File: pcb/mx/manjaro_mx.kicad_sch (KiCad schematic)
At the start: 93 parts, among them SW1 SW_Push, SW10 SW_Push, SW11 SW_Push, SW12 SW_Push, SW13 SW_Push, SW14 SW_Push, SW15 SW_Push, SW16 SW_Push, SW17 SW_Push, SW18 SW_Push, SW19 SW_Push, SW2 SW_Push, SW20 SW_Push, SW21 SW_Push, SW22 SW_Push, SW3 SW_Push, SW4 SW_Push, SW5 SW_Push, SW6 SW_Push, SW7 SW_Push, SW8 SW_Push, SW9 SW_Push, U1 XIAO-RP2040-DIP

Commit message: [V0] add jlcpcb files
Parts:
- BT1, rBT1, rJ3: now not fitted; now left out of the parts list
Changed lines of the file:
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@@
 		(unit 1)
 		(exclude_from_sim no)
-		(in_bom yes)
+		(in_bom no)
 		(on_board yes)
-		(dnp no)
+		(dnp yes)
 		(property "Reference" "rJ3"
 			(at 220.98 160.02 0)
@@
 		(unit 1)
 		(exclude_from_sim no)
-		(in_bom yes)
+		(in_bom no)
 		(on_board yes)
-		(dnp no)
+		(dnp yes)
 		(fields_autoplaced yes)
 		(property "Reference" "BT1"
@@
 		(unit 1)
 		(exclude_from_sim no)
-		(in_bom yes)
+		(in_bom no)
 		(on_board yes)
-		(dnp no)
+		(dnp yes)
 		(fields_autoplaced yes)
 		(property "Reference" "rBT1"

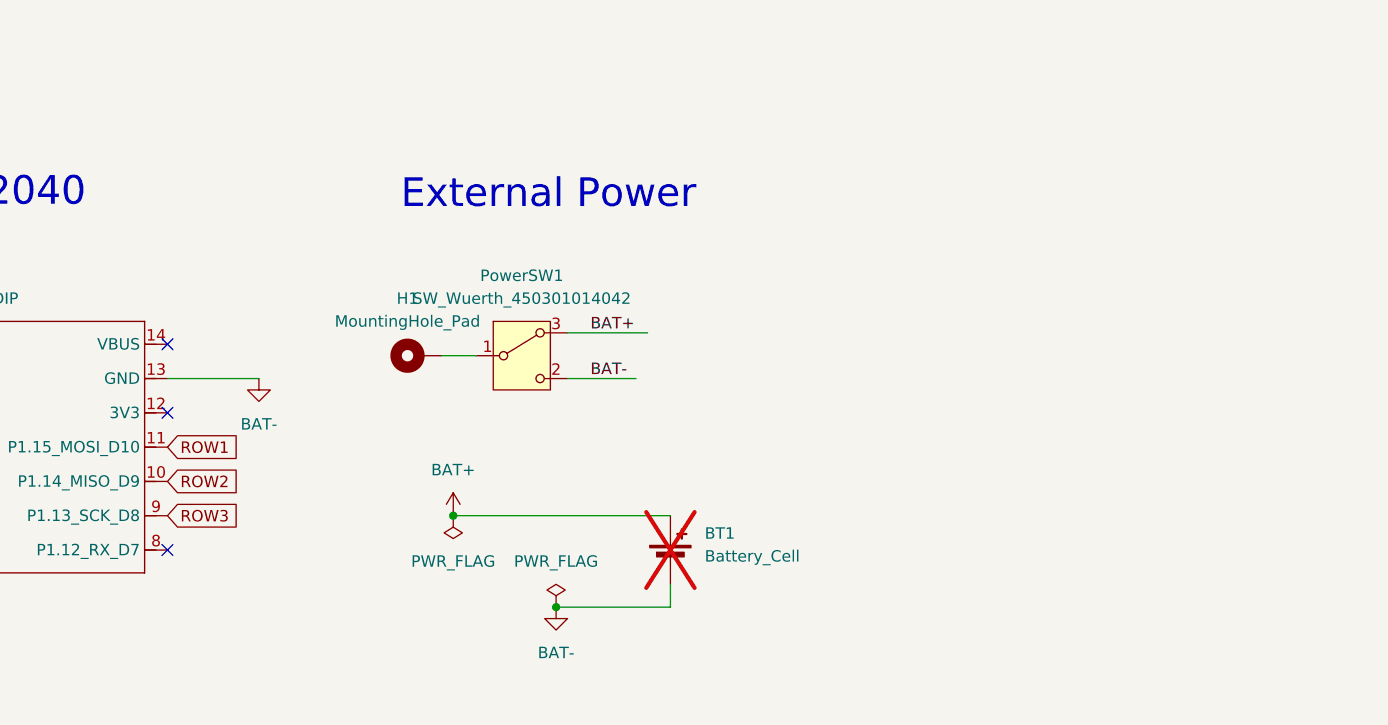
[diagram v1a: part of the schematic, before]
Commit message: [V0] Add TRRS conn for mint right
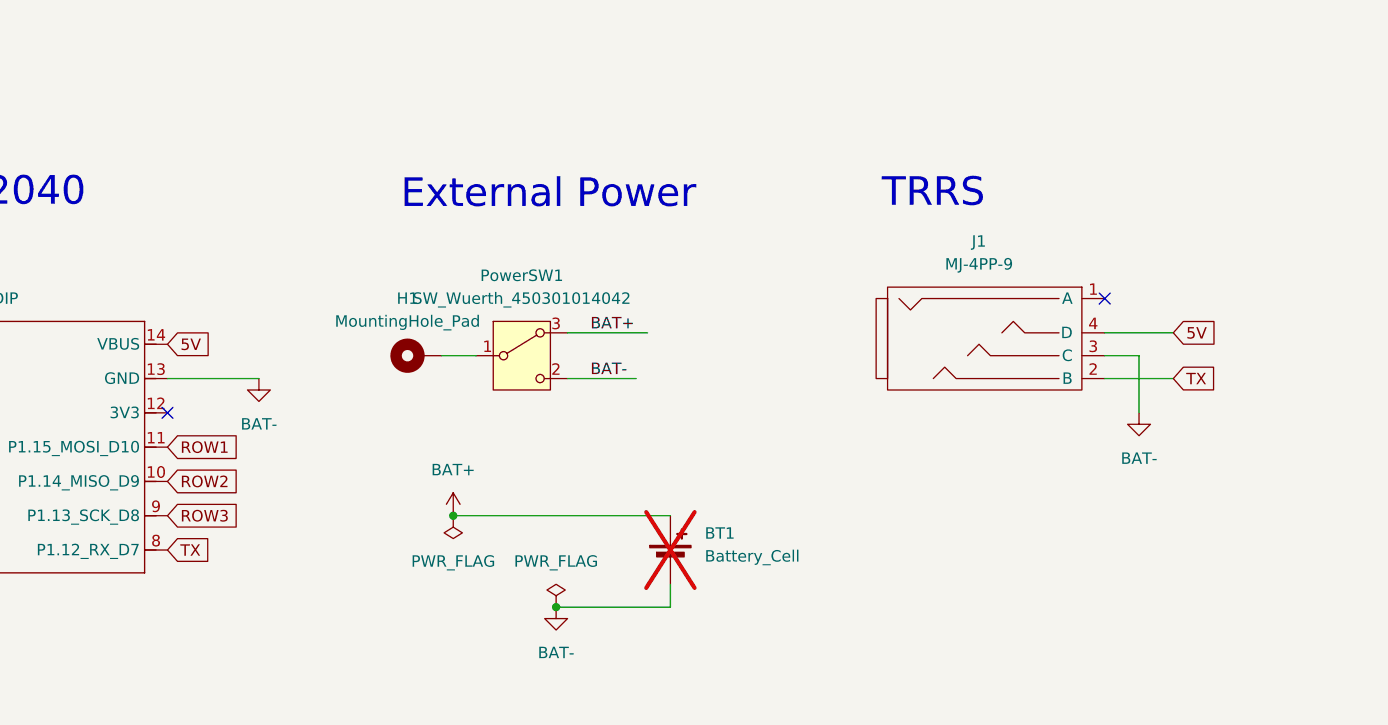
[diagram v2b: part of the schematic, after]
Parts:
- added J1: MJ-4PP-9, MJ-4PP-9:MJ-4PP-9, symbol MJ-4PP-9:MJ-4PP-9
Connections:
- net BAT-: now also J1.3 (C)
- net 5V: now reaches U1.14 (VBUS)
- net 5V: now also J1.4 (D)
- net TX: now reaches U1.8 (P1.12_RX_D7)
- net TX: now also J1.2 (B)
- no-connect marks 5 -> 4
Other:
- note added: "TRRS"

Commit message: Modify key layout
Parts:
- removed H1, H2: MountingHole_Pad, symbol Mechanical:MountingHole_Pad
- removed J1: MJ-4PP-9, MJ-4PP-9:MJ-4PP-9, symbol MJ-4PP-9:MJ-4PP-9
- removed U1, rU1: XIAO-RP2040-DIP, Seeed Studio XIAO Series Library:XIAO-RP2040-DIP, symbol Seeed_Studio_XIAO_Series:XIAO-nRF52840-DIP
- removed rD19, rD20: 1N4148WT, Diode_SMD:D_SOD-523, symbol Diode:1N4148WT
- removed rSW19, rSW20: SW_Push, kbd:keyswitch_cherrymx_hotswap_1u, symbol Switch:SW_Push
- added D23, D24, rD12, rD21, rD22, rD6: 1N4148WT, digikey-footprints:SOD-523, symbol Diode:1N4148WT
- added SW23, SW24, rSW12, rSW21, rSW22, rSW6: SW_Push, kbd_SW:CherryMX_Choc_Hotswap_1u, symbol Switch:SW_Push
- added U1, rU1: nice_nano, nice-nano-kicad:nice_nano, symbol nice_nano:nice_nano
- D1, D10, D11, D12, D13, D14, D15, D16, D17, D18, D19, D2, D20, D21, D22, D3, D4, D5, D6, D7, D8, D9, rD1, rD18, rD2, rD3, rD4, rD5: footprint Diode_SMD:D_SOD-523 -> digikey-footprints:SOD-523
- SW1, SW10, SW11, SW12, SW13, SW14, SW15, SW16, SW17, SW18, SW19, SW2, SW20, SW21, SW22, SW3, SW4, SW5, SW6, SW7, SW8, SW9, rSW1, rSW18, rSW2, rSW3, rSW4, rSW5: footprint kbd:keyswitch_cherrymx_hotswap_1u -> kbd_SW:CherryMX_Choc_Hotswap_1u
- rD10: renamed from rD9; footprint Diode_SMD:D_SOD-523 -> digikey-footprints:SOD-523
- rD11: renamed from rD10; footprint Diode_SMD:D_SOD-523 -> digikey-footprints:SOD-523
- rD13: renamed from rD11; footprint Diode_SMD:D_SOD-523 -> digikey-footprints:SOD-523
- rD14: renamed from rD12; footprint Diode_SMD:D_SOD-523 -> digikey-footprints:SOD-523
- rD15: renamed from rD13; footprint Diode_SMD:D_SOD-523 -> digikey-footprints:SOD-523
- rD16: renamed from rD14; footprint Diode_SMD:D_SOD-523 -> digikey-footprints:SOD-523
- rD17: renamed from rD15; footprint Diode_SMD:D_SOD-523 -> digikey-footprints:SOD-523
- rD19: renamed from rD16; footprint Diode_SMD:D_SOD-523 -> digikey-footprints:SOD-523
- rD20: renamed from rD17; footprint Diode_SMD:D_SOD-523 -> digikey-footprints:SOD-523
- rD7: renamed from rD6; footprint Diode_SMD:D_SOD-523 -> digikey-footprints:SOD-523
- rD8: renamed from rD7; footprint Diode_SMD:D_SOD-523 -> digikey-footprints:SOD-523
- rD9: renamed from rD8; footprint Diode_SMD:D_SOD-523 -> digikey-footprints:SOD-523
- rSW10: renamed from rSW9; footprint kbd:keyswitch_cherrymx_hotswap_1u -> kbd_SW:CherryMX_Choc_Hotswap_1u
- rSW11: renamed from rSW10; footprint kbd:keyswitch_cherrymx_hotswap_1u -> kbd_SW:CherryMX_Choc_Hotswap_1u
- rSW13: renamed from rSW11; footprint kbd:keyswitch_cherrymx_hotswap_1u -> kbd_SW:CherryMX_Choc_Hotswap_1u
- rSW14: renamed from rSW12; footprint kbd:keyswitch_cherrymx_hotswap_1u -> kbd_SW:CherryMX_Choc_Hotswap_1u
- rSW15: renamed from rSW13; footprint kbd:keyswitch_cherrymx_hotswap_1u -> kbd_SW:CherryMX_Choc_Hotswap_1u
- rSW16: renamed from rSW14; footprint kbd:keyswitch_cherrymx_hotswap_1u -> kbd_SW:CherryMX_Choc_Hotswap_1u
- rSW17: renamed from rSW15; footprint kbd:keyswitch_cherrymx_hotswap_1u -> kbd_SW:CherryMX_Choc_Hotswap_1u
- rSW19: renamed from rSW16; footprint kbd:keyswitch_cherrymx_hotswap_1u -> kbd_SW:CherryMX_Choc_Hotswap_1u
- rSW20: renamed from rSW17; footprint kbd:keyswitch_cherrymx_hotswap_1u -> kbd_SW:CherryMX_Choc_Hotswap_1u
- rSW7: renamed from rSW6; footprint kbd:keyswitch_cherrymx_hotswap_1u -> kbd_SW:CherryMX_Choc_Hotswap_1u
- rSW8: renamed from rSW7; footprint kbd:keyswitch_cherrymx_hotswap_1u -> kbd_SW:CherryMX_Choc_Hotswap_1u
- rSW9: renamed from rSW8; footprint kbd:keyswitch_cherrymx_hotswap_1u -> kbd_SW:CherryMX_Choc_Hotswap_1u
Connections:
- net BAT-: now also U1.23 (GND), U1.3 (GND), U1.4 (GND)
- net COL0: now also U1.7 (P0.22)
- net COL1: now also U1.8 (P0.24)
- net COL2: now also U1.9 (P1.00)
- net COL3: now also U1.10 (P0.11)
- net COL4: now also SW23.1, U1.11 (P1.04)
- net COL5: now also SW24.1, U1.12 (P1.06)
- net ROW0: now also U1.20 (AIN7/P0.31)
- net ROW1: now also U1.19 (AIN5/P0.29)
- net ROW2: now also U1.18 (AIN0/P0.02)
- net ROW3: now also D23.1 (K), D24.1 (K), U1.17 (P1.15)
- net SCLK: now also rU1.33 (P1.07)
- net SDIO: now also rU1.32 (P1.02)
- net rBAT-: now also rU1.23 (GND), rU1.3 (GND), rU1.4 (GND); no longer rJ3.5 (Pin_5)
- net rCOL0: now also rU1.7 (P0.22)
- net rCOL1: now also rU1.8 (P0.24)
- net rCOL2: now also rSW21.2, rU1.9 (P1.00); no longer rSW18.2
- net rCOL3: now also rSW22.2, rU1.10 (P0.11)
- net rCOL4: now also rU1.11 (P1.04)
- net rROW0: now also rD6.1 (K), rU1.20 (AIN7/P0.31)
- net rROW1: now also rD12.1 (K), rU1.19 (AIN5/P0.29)
- net rROW2: now also rD18.1 (K), rU1.18 (AIN0/P0.02)
- net rROW3: now also rD21.1 (K), rD22.1 (K), rU1.17 (P1.15); no longer rD18.1 (K)
- net at rPowerSW1.1 (B): now also rU1.24 (BATIN/P0.04)
- net at PowerSW1.1 (B): now also U1.24 (BATIN/P0.04)
- net 3V3 renamed r3V3
- net r3V3: now also rU1.21 (VCC)
- new net: rD12.2 (A), rSW12.1
- new net: rD21.2 (A), rSW21.1
- new net: D24.2 (A), SW24.2
- new net: D23.2 (A), SW23.2
- new net: rD6.2 (A), rSW6.1
- new net: rD22.2 (A), rSW22.1
- new net nCS: rJ3.5 (Pin_5), rU1.31 (P1.01)
- new net rCOL5: rSW12.2, rSW18.2, rSW6.2, rU1.12 (P1.06)
- no-connect marks 4 -> 23
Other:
- note added: "Nice NANO"
- note removed: "TRRS"
- note removed: "XIAO RP2040"
- moved on the sheet: BT1, PowerSW1, rBT1, rJ3, rPowerSW1

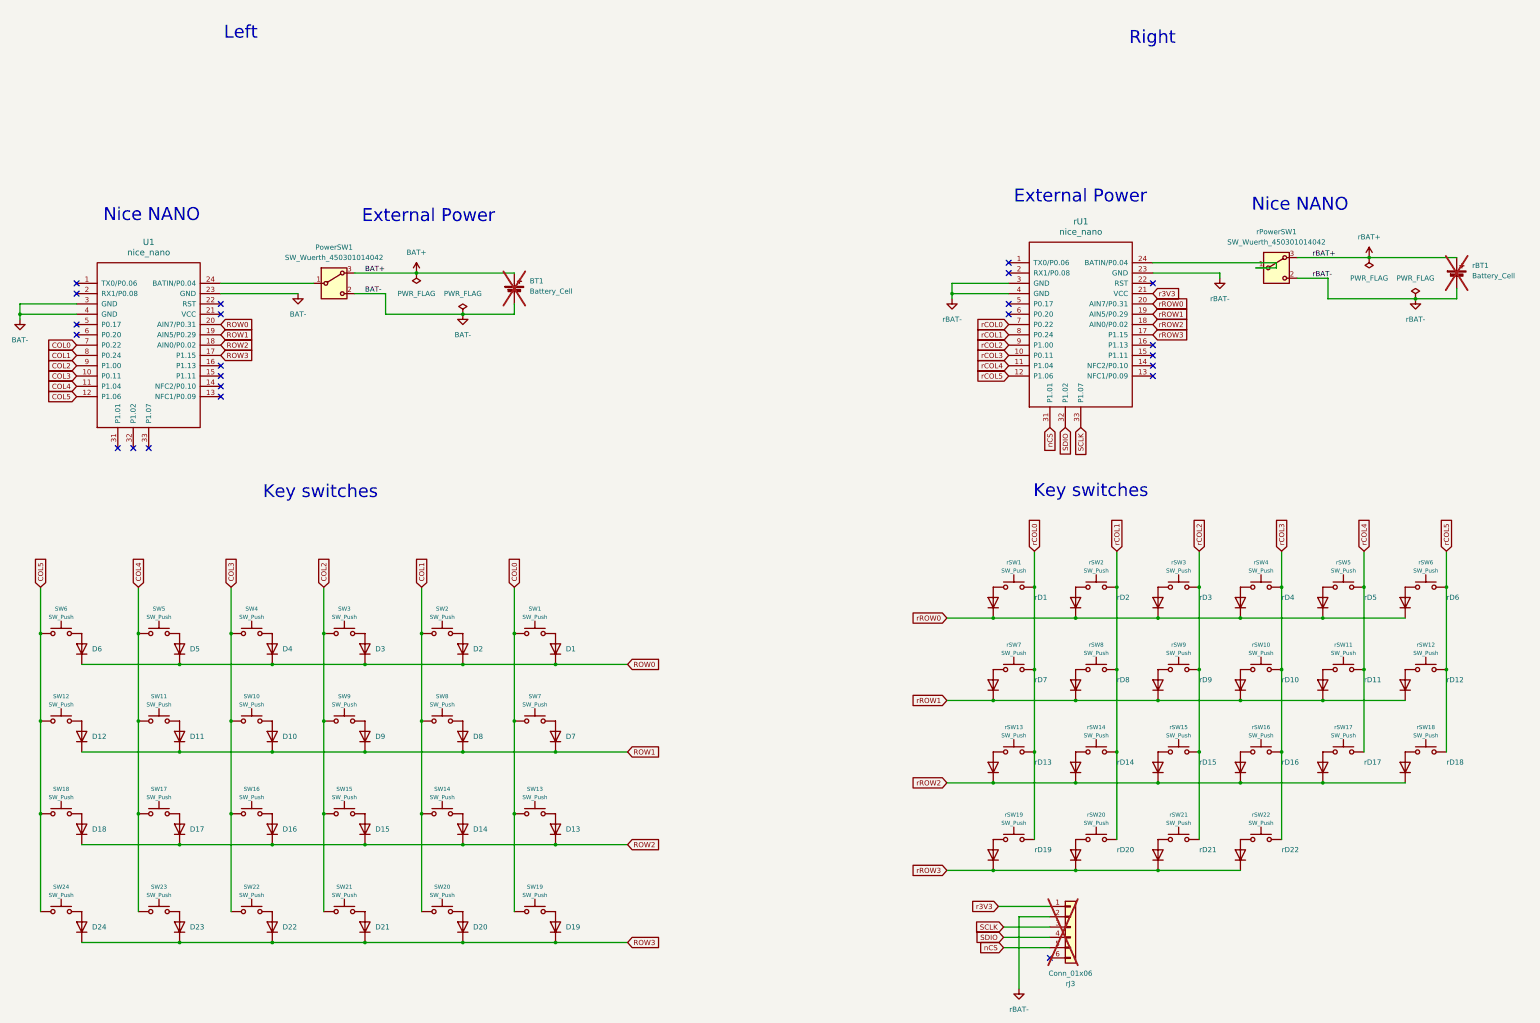
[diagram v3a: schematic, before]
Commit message: Modify MCU position
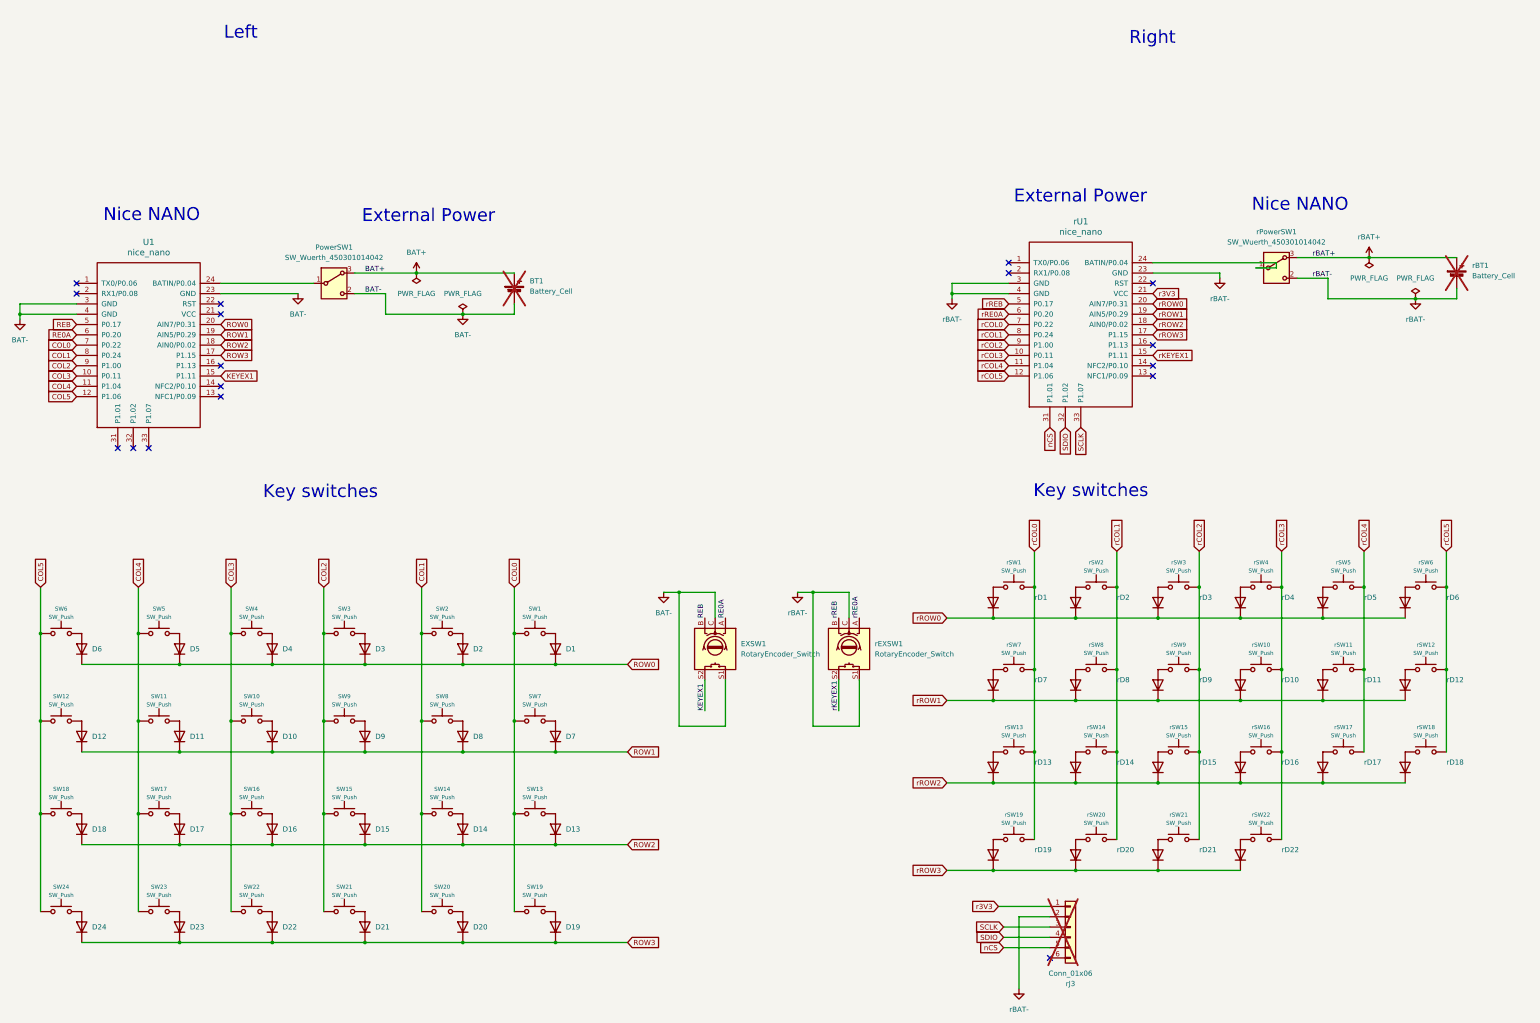
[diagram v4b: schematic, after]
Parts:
- added EXSW1, rEXSW1: RotaryEncoder_Switch, Keebio-Parts:RotaryEncoder_EC11, symbol Device:RotaryEncoder_Switch
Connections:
- net BAT-: now also EXSW1.C, EXSW1.S1
- net rBAT-: now also rEXSW1.C, rEXSW1.S1
- net rKEYEX1: now reaches rU1.15 (P1.11)
- net rKEYEX1: now also rEXSW1.S2
- net rREB: now reaches rU1.5 (P0.17)
- net rREB: now also rEXSW1.B
- net rRE0A: now reaches rU1.6 (P0.20)
- net rRE0A: now also rEXSW1.A
- net KEYEX1: now reaches U1.15 (P1.11)
- net KEYEX1: now also EXSW1.S2
- net REB: now reaches U1.5 (P0.17)
- net REB: now also EXSW1.B
- net RE0A: now reaches U1.6 (P0.20)
- net RE0A: now also EXSW1.A
- no-connect marks 23 -> 17

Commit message: fixed external line
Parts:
- removed EXSW1, rEXSW1: RotaryEncoder_Switch, Keebio-Parts:RotaryEncoder_EC11, symbol Device:RotaryEncoder_Switch
- D1, D10, D11, D12, D13, D14, D15, D16, D17, D18, D19, D2, D20, D21, D22, D23, D24, D3, D4, D5, D6, D7, D8, D9, rD1, rD10, rD11, rD12, rD13, rD14, rD15, rD16, rD17, rD18, rD19, rD2, rD20, rD21, rD22, rD3, rD4, rD5, rD6, rD7, rD8, rD9: footprint digikey-footprints:SOD-523 -> Keebio-Parts:D_SOD-323
- SW1, SW10, SW11, SW12, SW13, SW14, SW15, SW16, SW17, SW18, SW19, SW2, SW20, SW21, SW22, SW23, SW24, SW3, SW4, SW5, SW6, SW7, SW8, SW9, rSW1, rSW10, rSW11, rSW12, rSW13, rSW14, rSW15, rSW16, rSW17, rSW18, rSW19, rSW2, rSW20, rSW21, rSW22, rSW3, rSW4, rSW5, rSW6, rSW7, rSW8, rSW9: footprint kbd_SW:CherryMX_Choc_Hotswap_1u -> kbd_SW:Choc_Hotswap_1u
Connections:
- net KEYEX1: no longer names the net of U1.15 (P1.11)
- net RE0A: no longer names the net of U1.6 (P0.20)
- net REB: no longer names the net of U1.5 (P0.17)
- net rKEYEX1: no longer names the net of rU1.15 (P1.11)
- net rRE0A: no longer names the net of rU1.6 (P0.20)
- net rREB: no longer names the net of rU1.5 (P0.17)
- no-connect marks 17 -> 23
